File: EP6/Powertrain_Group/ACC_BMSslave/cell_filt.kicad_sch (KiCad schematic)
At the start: 4 parts

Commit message: ACC_BMSslave pcb priliminary layout
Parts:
- C31: footprint Capacitor_SMD:C_0603_1608Metric -> Capacitor_SMD:C_0805_2012Metric
- C32: footprint Capacitor_SMD:C_0603_1608Metric -> Capacitor_SMD:C_0402_1005Metric
- R71: footprint Resistor_SMD:R_0603_1608Metric -> Resistor_SMD:R_0402_1005Metric
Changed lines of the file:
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@@
 			)
 		)
-		(property "Footprint" "Capacitor_SMD:C_0603_1608Metric"
+		(property "Footprint" "Capacitor_SMD:C_0402_1005Metric"
 			(at 130.5052 102.87 0)
 			(effects
@@
 			)
 		)
-		(property "Footprint" "Resistor_SMD:R_0603_1608Metric"
+		(property "Footprint" "Resistor_SMD:R_0402_1005Metric"
 			(at 104.14 91.948 90)
 			(effects
@@
 			)
 		)
-		(property "Footprint" "Capacitor_SMD:C_0603_1608Metric"
+		(property "Footprint" "Capacitor_SMD:C_0805_2012Metric"
 			(at 112.7252 99.06 0)
 			(effects

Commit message: [BMSslave] snapshot
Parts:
- renumbered R71 to R73
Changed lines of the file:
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@@
 		(shape input)
 		(at 147.32 90.17 0)
-		(fields_autoplaced yes)
 		(effects
 			(font
@@
 		(shape input)
 		(at 147.32 107.95 0)
-		(fields_autoplaced yes)
 		(effects
 			(font
@@
 		(shape input)
 		(at 97.79 90.17 180)
-		(fields_autoplaced yes)
 		(effects
 			(font
@@
 		(dnp no)
 		(fields_autoplaced yes)
-		(property "Reference" "R71"
+		(property "Reference" "R73"
 			(at 104.14 83.82 90)
 			(effects
@@
 			(project "BMS_Slave_V1(ADBMS1818)"
 				(path "/0942010f-46b1-4fe9-9f5e-a3ebd22b3e41/0e012c4e-db98-4388-8085-d52e2eb08c8e"
-					(reference "R71")
+					(reference "R73")
 					(unit 1)
 				)
 				(path "/0942010f-46b1-4fe9-9f5e-a3ebd22b3e41/0e32dbbe-90fa-4150-b676-8af18ab9fc88"
-					(reference "R97")
+					(reference "R99")
 					(unit 1)
 				)
 				(path "/0942010f-46b1-4fe9-9f5e-a3ebd22b3e41/140713f3-b752-488c-9623-85002c7af827"
-					(reference "R86")
+					(reference "R88")
 					(unit 1)
 				)
 				(path "/0942010f-46b1-4fe9-9f5e-a3ebd22b3e41/1ddf4a32-8b4f-49cc-9c4a-4d3d90e5079a"
-					(reference "R81")
+					(reference "R83")
 					(unit 1)
 				)
 				(path "/0942010f-46b1-4fe9-9f5e-a3ebd22b3e41/25d98cfb-cd04-4e07-9a04-b81b51b8a500"
-					(reference "R102")
+					(reference "R104")
 					(unit 1)
 				)
 				(path "/0942010f-46b1-4fe9-9f5e-a3ebd22b3e41/3b09feb8-37a6-487e-a8a0-19aebf7accdf"
+					(reference "R127")
+					(unit 1)
+				)
+				(path "/0942010f-46b1-4fe9-9f5e-a3ebd22b3e41/504d3791-7cfe-4fbc-a88c-ccf77f103d87"
+					(reference "R78")
+					(unit 1)
+				)
+				(path "/0942010f-46b1-4fe9-9f5e-a3ebd22b3e41/7e18990b-3ea3-4bef-8a4c-880e7dab41da"
+					(reference "R98")
+					(unit 1)
+				)
+				(path "/0942010f-46b1-4fe9-9f5e-a3ebd22b3e41/8a14b701-4145-414f-9288-5a43a13b4396"
 					(reference "R125")
 					(unit 1)
 				)
-				(path "/0942010f-46b1-4fe9-9f5e-a3ebd22b3e41/504d3791-7cfe-4fbc-a88c-ccf77f103d87"
-					(reference "R76")
-					(unit 1)
-				)
-				(path "/0942010f-46b1-4fe9-9f5e-a3ebd22b3e41/7e18990b-3ea3-4bef-8a4c-880e7dab41da"
-					(reference "R96")
-					(unit 1)
-				)
-				(path "/0942010f-46b1-4fe9-9f5e-a3ebd22b3e41/8a14b701-4145-414f-9288-5a43a13b4396"
-					(reference "R123")
-					(unit 1)
-				)
 				(path "/0942010f-46b1-4fe9-9f5e-a3ebd22b3e41/9b95d718-7b7f-4d39-88a5-a9af9f53e1cb"
-					(reference "R66")
+					(reference "R68")
 					(unit 1)
 				)
 				(path "/0942010f-46b1-4fe9-9f5e-a3ebd22b3e41/b001d3fa-c156-4a0a-b429-3e27986f1785"
+					(reference "R128")
+					(unit 1)
+				)
+				(path "/0942010f-46b1-4fe9-9f5e-a3ebd22b3e41/d4eee729-ec8c-4be7-9853-a2241d31c9cf"
+					(reference "R63")
+					(unit 1)
+				)
+				(path "/0942010f-46b1-4fe9-9f5e-a3ebd22b3e41/e43d0643-8a1f-4f27-b691-eaa389158ca9"
 					(reference "R126")
 					(unit 1)
 				)
-				(path "/0942010f-46b1-4fe9-9f5e-a3ebd22b3e41/d4eee729-ec8c-4be7-9853-a2241d31c9cf"
-					(reference "R61")
-					(unit 1)
-				)
-				(path "/0942010f-46b1-4fe9-9f5e-a3ebd22b3e41/e43d0643-8a1f-4f27-b691-eaa389158ca9"
-					(reference "R124")
-					(unit 1)
-				)
 				(path "/0942010f-46b1-4fe9-9f5e-a3ebd22b3e41/e5d2fee0-662b-4492-aa1a-322340b04f57"
-					(reference "R91")
+					(reference "R93")
 					(unit 1)
 				)
 				(path "/0942010f-46b1-4fe9-9f5e-a3ebd22b3e41/fbc34dc8-7c98-45f0-a6cb-6b0033b2f965"
-					(reference "R127")
+					(reference "R129")
 					(unit 1)
 				)
@@
 		(dnp no)
 		(fields_autoplaced yes)
-		(property "Reference" "#PWR077"
+		(property "Reference" "#PWR057"
 			(at 111.76 107.95 0)
 			(effects
@@
 			(project "BMS_Slave_V1(ADBMS1818)"
 				(path "/0942010f-46b1-4fe9-9f5e-a3ebd22b3e41/0e012c4e-db98-4388-8085-d52e2eb08c8e"
-					(reference "#PWR077")
+					(reference "#PWR057")
 					(unit 1)
 				)
 				(path "/0942010f-46b1-4fe9-9f5e-a3ebd22b3e41/0e32dbbe-90fa-4150-b676-8af18ab9fc88"
-					(reference "#PWR083")
+					(reference "#PWR063")
 					(unit 1)
 				)
 				(path "/0942010f-46b1-4fe9-9f5e-a3ebd22b3e41/140713f3-b752-488c-9623-85002c7af827"
-					(reference "#PWR080")
+					(reference "#PWR060")
 					(unit 1)
 				)
 				(path "/0942010f-46b1-4fe9-9f5e-a3ebd22b3e41/1ddf4a32-8b4f-49cc-9c4a-4d3d90e5079a"
-					(reference "#PWR079")
+					(reference "#PWR059")
 					(unit 1)
 				)
 				(path "/0942010f-46b1-4fe9-9f5e-a3ebd22b3e41/25d98cfb-cd04-4e07-9a04-b81b51b8a500"
-					(reference "#PWR084")
+					(reference "#PWR064")
 					(unit 1)
 				)
 				(path "/0942010f-46b1-4fe9-9f5e-a3ebd22b3e41/3b09feb8-37a6-487e-a8a0-19aebf7accdf"
-					(reference "#PWR087")
+					(reference "#PWR067")
 					(unit 1)
 				)
 				(path "/0942010f-46b1-4fe9-9f5e-a3ebd22b3e41/504d3791-7cfe-4fbc-a88c-ccf77f103d87"
-					(reference "#PWR078")
+					(reference "#PWR058")
 					(unit 1)
 				)
 				(path "/0942010f-46b1-4fe9-9f5e-a3ebd22b3e41/7e18990b-3ea3-4bef-8a4c-880e7dab41da"
-					(reference "#PWR082")
+					(reference "#PWR062")
 					(unit 1)
 				)
 				(path "/0942010f-46b1-4fe9-9f5e-a3ebd22b3e41/8a14b701-4145-414f-9288-5a43a13b4396"
-					(reference "#PWR085")
+					(reference "#PWR065")
 					(unit 1)
 				)
 				(path "/0942010f-46b1-4fe9-9f5e-a3ebd22b3e41/9b95d718-7b7f-4d39-88a5-a9af9f53e1cb"
-					(reference "#PWR076")
+					(reference "#PWR056")
 					(unit 1)
 				)
 				(path "/0942010f-46b1-4fe9-9f5e-a3ebd22b3e41/b001d3fa-c156-4a0a-b429-3e27986f1785"
-					(reference "#PWR088")
+					(reference "#PWR068")
 					(unit 1)
 				)
 				(path "/0942010f-46b1-4fe9-9f5e-a3ebd22b3e41/d4eee729-ec8c-4be7-9853-a2241d31c9cf"
-					(reference "#PWR075")
+					(reference "#PWR055")
 					(unit 1)
 				)
 				(path "/0942010f-46b1-4fe9-9f5e-a3ebd22b3e41/e43d0643-8a1f-4f27-b691-eaa389158ca9"
-					(reference "#PWR086")
+					(reference "#PWR066")
 					(unit 1)
 				)
 				(path "/0942010f-46b1-4fe9-9f5e-a3ebd22b3e41/e5d2fee0-662b-4492-aa1a-322340b04f57"
-					(reference "#PWR081")
+					(reference "#PWR061")
 					(unit 1)
 				)
 				(path "/0942010f-46b1-4fe9-9f5e-a3ebd22b3e41/fbc34dc8-7c98-45f0-a6cb-6b0033b2f965"
-					(reference "#PWR089")
-					(unit 1)
-				)
+					(reference "#PWR069")
+					(unit 1)
+				)

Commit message: [BMSslave] snapshot
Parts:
- renumbered C31 to C27, C32 to C28, R73 to R60, Z3 to Z1

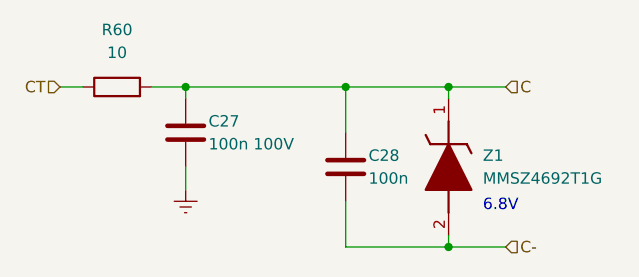
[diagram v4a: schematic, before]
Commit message: update ACC_BMSslave to V3.1
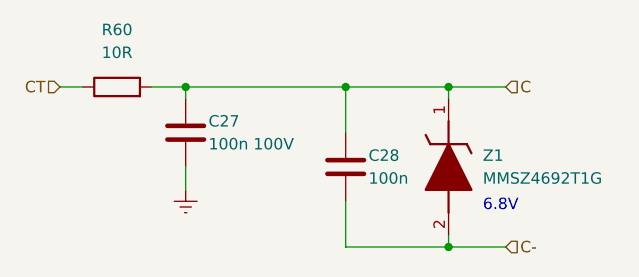
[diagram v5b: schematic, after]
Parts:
- R60: value 10 -> 10R
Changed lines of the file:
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@@
 			)
 		)
-		(property "Value" "10"
+		(property "Value" "10R"
 			(at 104.14 86.36 90)
 			(effects
